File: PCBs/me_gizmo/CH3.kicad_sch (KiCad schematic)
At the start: 10 parts, among them J3 PushButton_Terminal_01x06, U1 ADG714, U3 ADG714, U4 ADG714

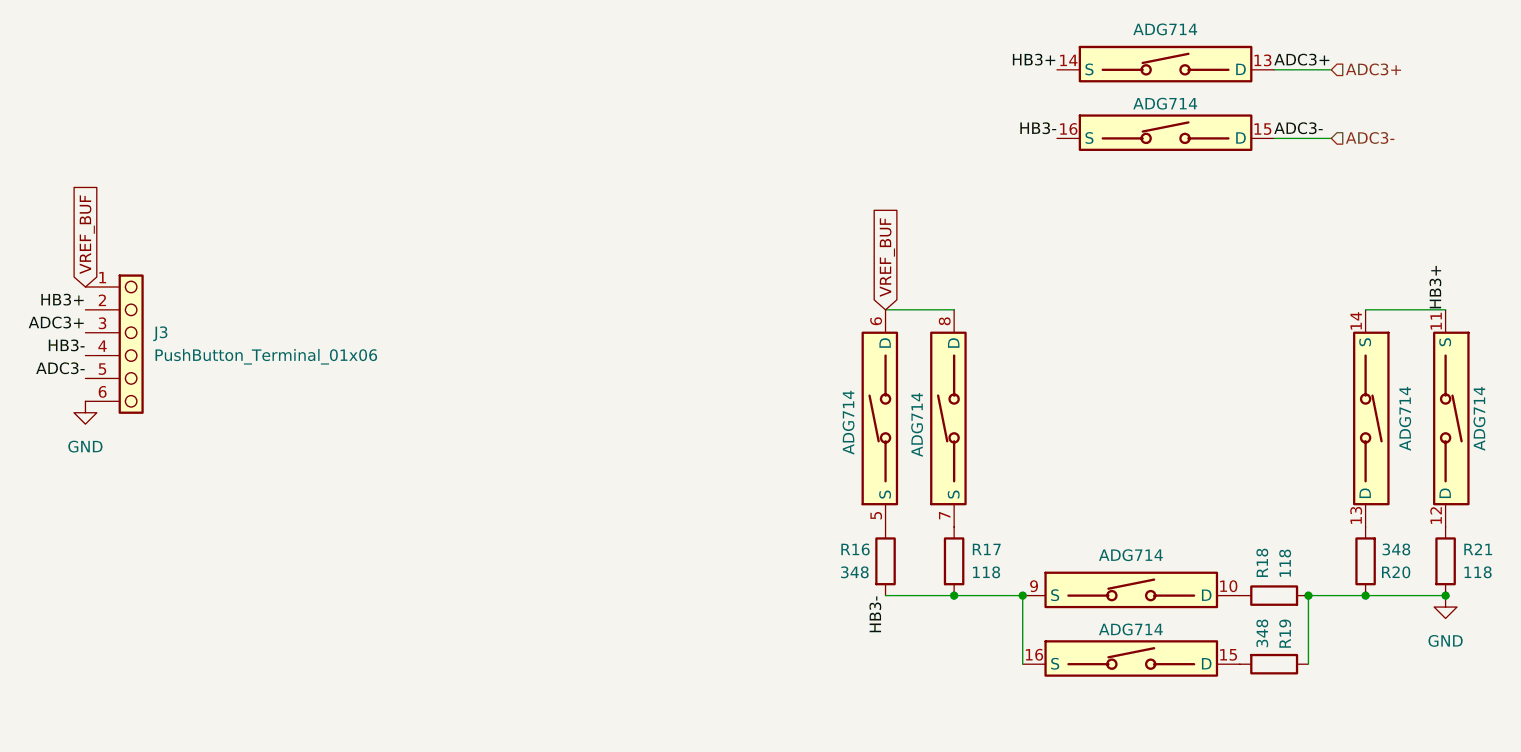
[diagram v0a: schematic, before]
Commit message: Completed first draft of integrated measurement unit
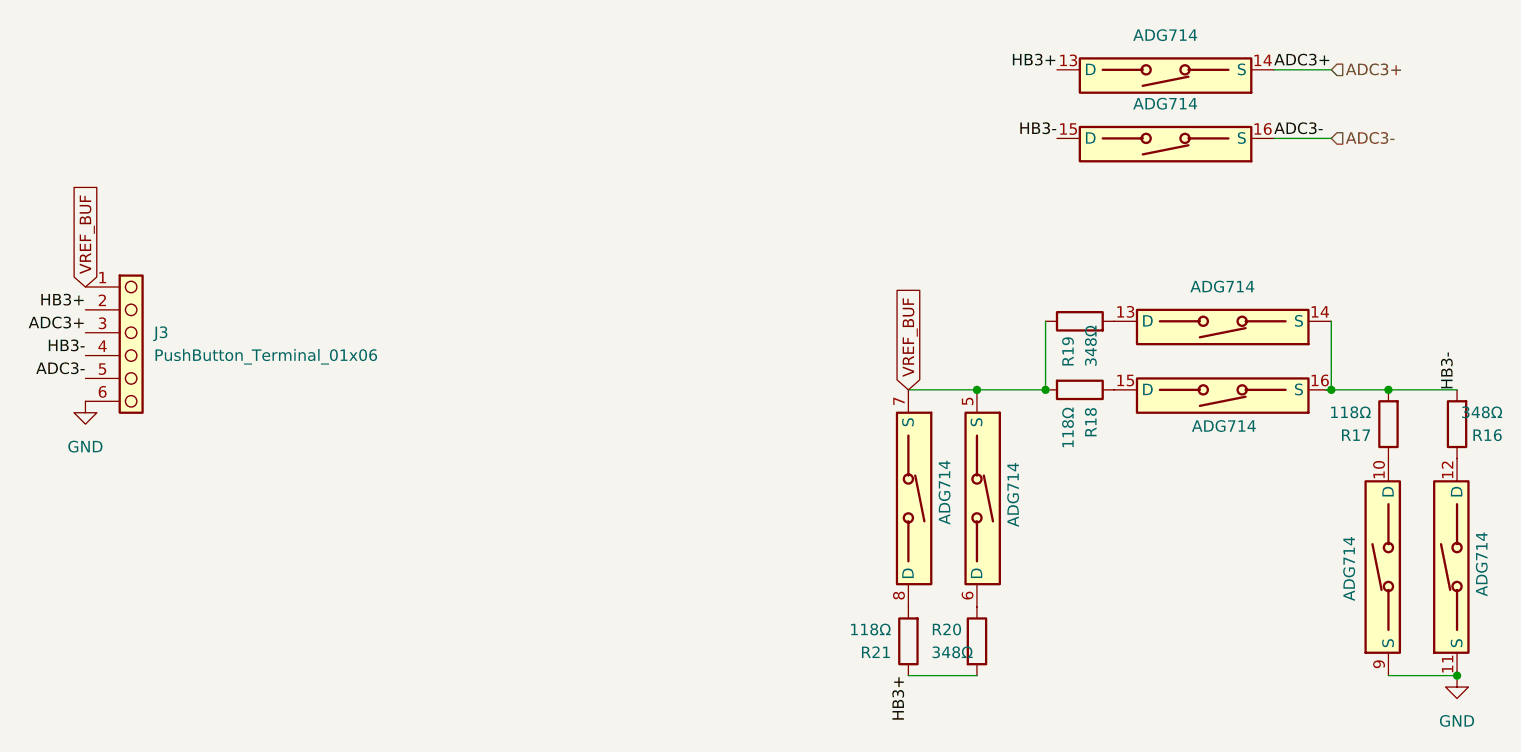
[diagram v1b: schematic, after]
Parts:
- J3: footprint WAGO:CONN5_233-505_WAG -> TerminalBlock_WAGO:TerminalBlock_WAGO_233-506_2x06_P2.54mm
- R16, R19, R20: value 348 -> 348Ω
- R17, R18, R21: value 118 -> 118Ω
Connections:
- net ADC3+: now also U3.14 (S); no longer U3.13 (D)
- net ADC3-: now also U3.16 (S); no longer U3.15 (D)
- net GND: now also U4.11 (S), U4.9 (S); no longer R18.2, R19.1, R20.1, R21.2
- net HB3+: now also R20.2, R21.1, U3.13 (D); no longer U3.14 (S), U4.11 (S), U4.14 (S)
- net HB3-: now also U3.15 (D), U4.14 (S); no longer U3.16 (S), U4.9 (S)
- net VREF_BUF: now also R18.2, R19.1, U1.5 (S), U1.7 (S); no longer U1.6 (D), U1.8 (D)
- net at R16.1: now also U4.12 (D); no longer U1.5 (S)
- net at U4.13 (D): now also R19.2; no longer R20.2
- net at R18.1: now also U4.15 (D); no longer U4.10 (D)
- net at R17.1: now also U4.10 (D); no longer U1.7 (S)
- new net: R20.1, U1.6 (D)
- new net: R21.2, U1.8 (D)
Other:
- moved on the sheet: R16, R17, R18, R19, R20, R21

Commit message: Second draft of final layout
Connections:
- net HB3+: now also R16.2, R17.2, U4.14 (S), U4.16 (S); no longer R20.2, R21.1
- net HB3-: now also R20.2, R21.1; no longer R16.2, R17.2, U4.14 (S), U4.16 (S)
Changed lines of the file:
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@@
 	)
 	(label "HB3+"
-		(at 154.94 134.62 270)
+		(at 215.9 102.87 90)
 		(effects
 			(font
 				(size 1.27 1.27)
 			)
-			(justify right bottom)
+			(justify left bottom)
 		)
 	)
@@
 	)
 	(label "HB3-"
-		(at 215.9 102.87 90)
+		(at 154.94 134.62 270)
 		(effects
 			(font
 				(size 1.27 1.27)
 			)
-			(justify left bottom)
+			(justify right bottom)
 		)
 	)
